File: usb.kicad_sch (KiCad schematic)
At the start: 29 parts, among them J3 USB4105-GF-A, U11 TPD4E05U06QDQARQ1, U5 FT230X, U8 NCP730BMT330

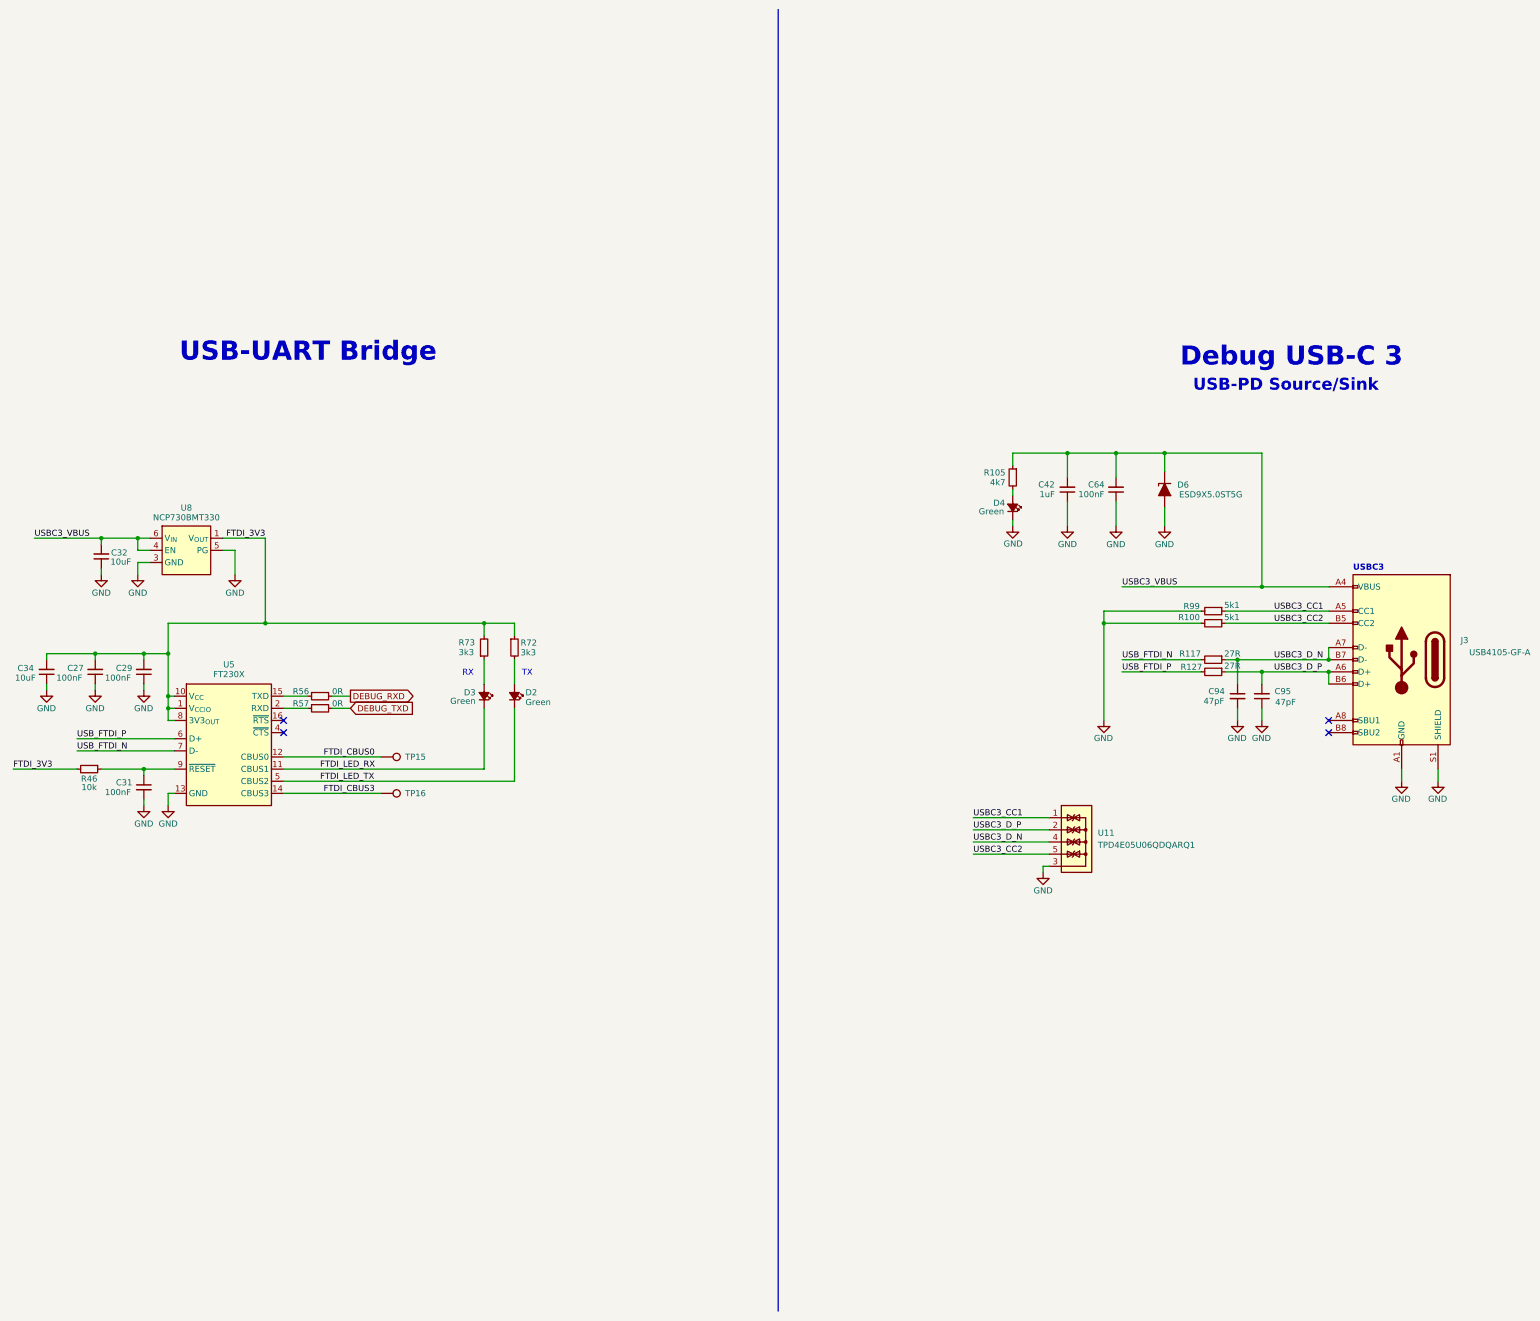
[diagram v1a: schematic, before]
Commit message: Finish HDMI routing, replace usbc w/ usba
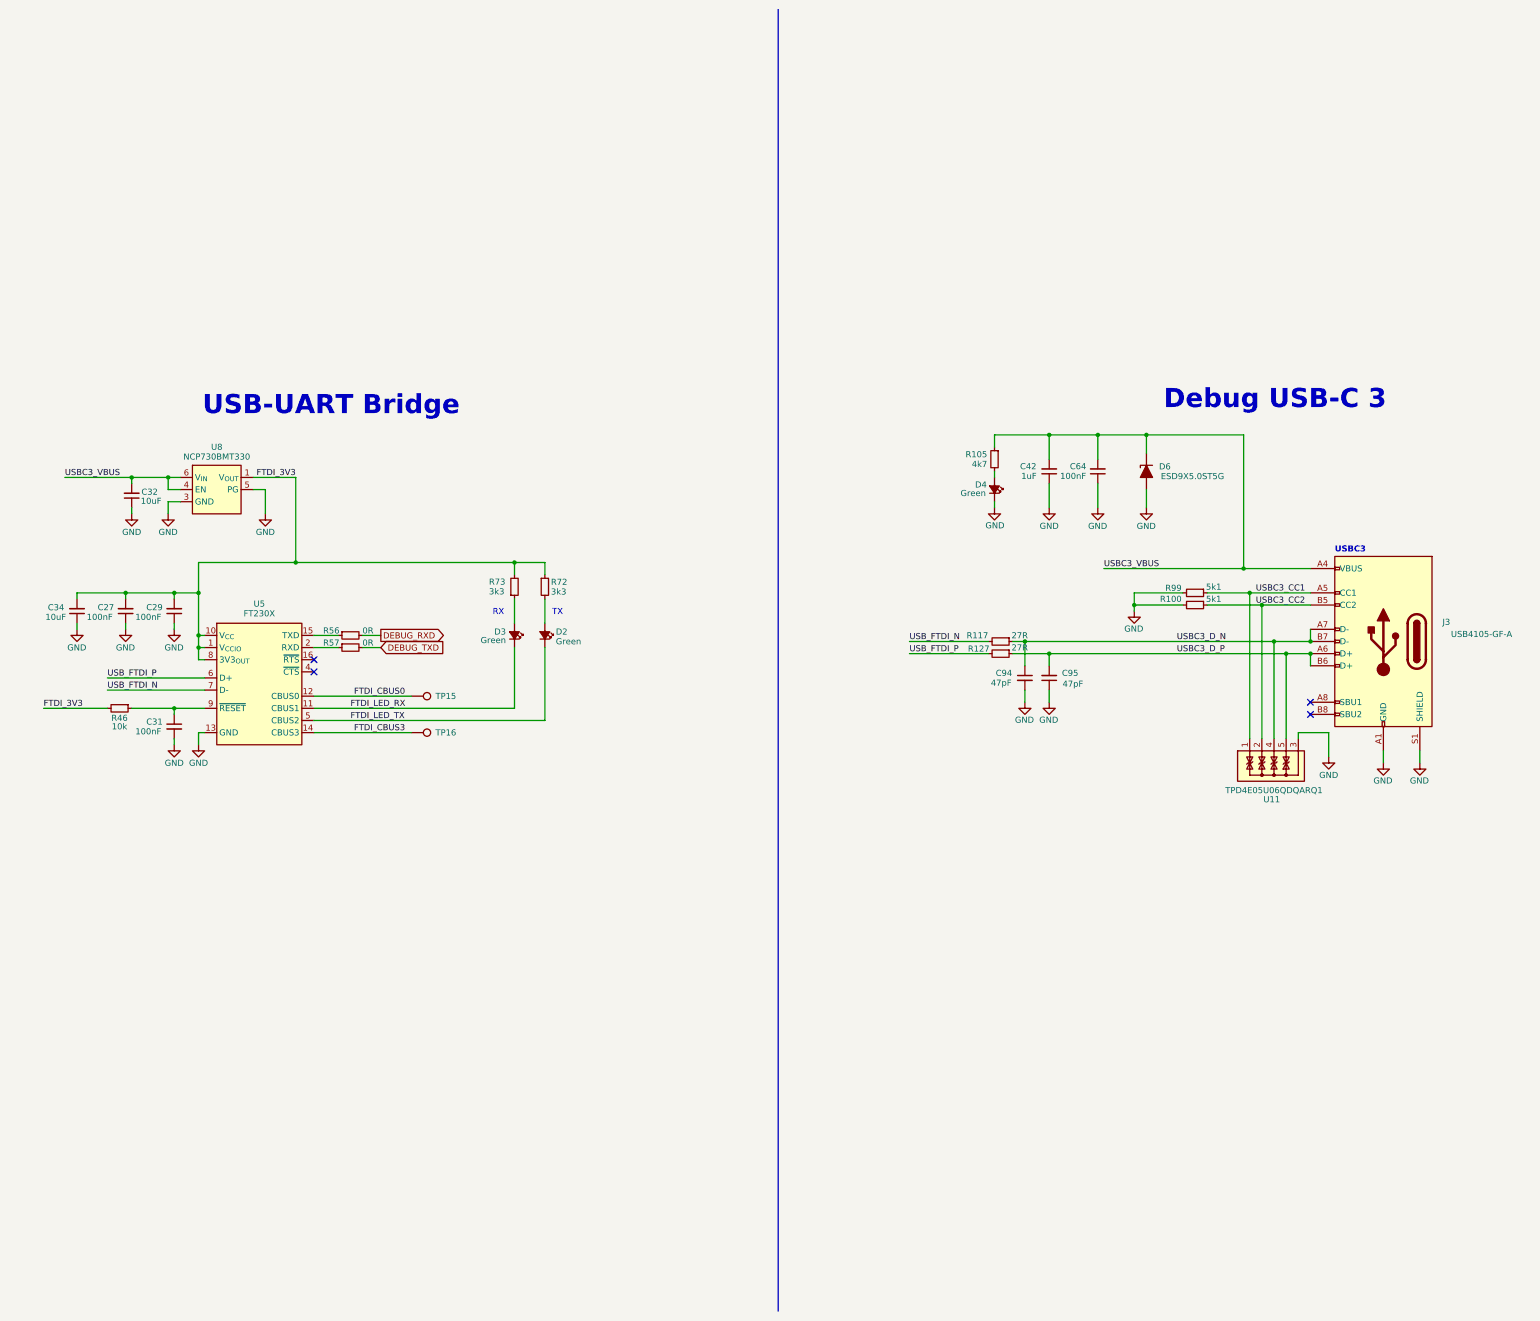
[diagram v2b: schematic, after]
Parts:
- U11: footprint JetsonCarrier:USON-10_2.5x1mm_P0.5mm -> Argus-Miscellaneous:USON-10_TEX
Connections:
- net USBC3_CC2: now also U11.2, U11.9; no longer U11.5, U11.6
- net USBC3_D_P: now also U11.5, U11.6; no longer U11.2, U11.9
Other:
- note removed: "USB-PD Source/Sink"
